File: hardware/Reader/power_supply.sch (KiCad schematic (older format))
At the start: 4 parts

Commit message: Revising reader
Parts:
- added J_PS_2, J_PS_3: 1546931-2, footprints:1546931-2, symbol 1546931-2:1546931-2
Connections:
- net +12V: now also J_PS_1.1
- net +3V3: now also J_PS_3.1; no longer J_PS_1.2
- net +5V: now also J_PS_2.1; no longer J_PS_1.1
- net GND: now also J_PS_1.2, J_PS_2.2, J_PS_3.2
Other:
- moved on the sheet: J_PS_1
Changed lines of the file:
@@
 $Descr USLetter 11000 8500
 encoding utf-8
-Sheet 15 19
+Sheet 13 19
 Title "CANnect Reader | Power Supply"
-Date "2020-10-28"
-Rev "0.0.04"
+Date "2020-11-19"
+Rev "0.0.05"
 Comp "CANtech"
 Comment1 "Created by Choong Jin Ng | jin8383@gmail.com"
@@
 $EndComp
 Wire Wire Line
-	3350 3500 3350 4350
+	3350 3500 3350 3700
 $Sheet
 S 1700 2450 1500 750
@@
 	6850 3550 6850 3400
 Wire Wire Line
-	6850 2500 6850 2350
-Wire Wire Line
 	6850 4000 6850 3850
 $Comp
@@
 NoConn ~ 6450 2000
 Connection ~ 6850 3400
-Wire Wire Line
-	7250 3400 7250 2600
-Wire Wire Line
-	6850 3400 7250 3400
 Connection ~ 6850 1900
-Wire Wire Line
-	7250 1900 7250 2500
-Wire Wire Line
-	6850 1900 7250 1900
 Wire Wire Line
 	6850 1900 6850 1650
@@
 L 1546931-2:1546931-2 J_PS_1
 U 1 1 5FA002EC
-P 7850 2600
-F 0 "J_PS_1" H 8080 2696 50  0000 L CNN
-F 1 "1546931-2" H 8080 2605 50  0000 L CNN
-F 2 "footprints:1546931-2" H 7850 2600 50  0001 L BNN
-F 3 "https://www.te.com/commerce/DocumentDelivery/DDEController?Action=srchrtrv&DocNm=1-1773458-1_EURO_STYLE_QRG&DocType=DS&DocLang=English" H 7850 2600 50  0001 L BNN
-F 4 "1546931-2" H 7850 2600 50  0001 C CNN "Part Name"
-F 5 "TE Connectivity AMP Connectors" H 7850 2600 50  0001 C CNN "Manufacturer"
-F 6 "Digikey Canada" H 7850 2600 50  0001 C CNN "Vendor"
-F 7 "A97965-ND" H 7850 2600 50  0001 C CNN "digikeypn"
-	1    7850 2600
-	1    0    0    -1
-$EndComp
-Wire Wire Line
-	7250 2500 7450 2500
-Wire Wire Line
-	7450 2600 7250 2600
-Wire Wire Line
-	3350 2800 4850 2800
+P 4250 3700
+F 0 "J_PS_1" H 4480 3796 50  0000 L CNN
+F 1 "1546931-2" H 4480 3705 50  0000 L CNN
+F 2 "footprints:1546931-2" H 4250 3700 50  0001 L BNN
+F 3 "https://www.te.com/commerce/DocumentDelivery/DDEController?Action=srchrtrv&DocNm=1-1773458-1_EURO_STYLE_QRG&DocType=DS&DocLang=English" H 4250 3700 50  0001 L BNN
+F 4 "1546931-2" H 4250 3700 50  0001 C CNN "Part Name"
+F 5 "TE Connectivity AMP Connectors" H 4250 3700 50  0001 C CNN "Manufacturer"
+F 6 "Digikey Canada" H 4250 3700 50  0001 C CNN "Vendor"
+F 7 "A97965-ND" H 4250 3700 50  0001 C CNN "digikeypn"
+	1    4250 3700
+	1    0    0    -1
+$EndComp
+Wire Wire Line
+	3350 2800 3850 2800
 Wire Wire Line
 	3300 5150 6000 5150
+$Comp
+L 1546931-2:1546931-2 J_PS_2
+U 1 1 5FBD8B3B
+P 7850 2000
+F 0 "J_PS_2" H 8080 2096 50  0000 L CNN
+F 1 "1546931-2" H 8080 2005 50  0000 L CNN
+F 2 "footprints:1546931-2" H 7850 2000 50  0001 L BNN
+F 3 "https://www.te.com/commerce/DocumentDelivery/DDEController?Action=srchrtrv&DocNm=1-1773458-1_EURO_STYLE_QRG&DocType=DS&DocLang=English" H 7850 2000 50  0001 L BNN
+F 4 "1546931-2" H 7850 2000 50  0001 C CNN "Part Name"
+F 5 "TE Connectivity AMP Connectors" H 7850 2000 50  0001 C CNN "Manufacturer"
+F 6 "Digikey Canada" H 7850 2000 50  0001 C CNN "Vendor"
+F 7 "A97965-ND" H 7850 2000 50  0001 C CNN "digikeypn"
+	1    7850 2000
+	1    0    0    -1
+$EndComp
+$Comp
+L 1546931-2:1546931-2 J_PS_3
+U 1 1 5FBD9454
+P 7850 3500
+F 0 "J_PS_3" H 8080 3596 50  0000 L CNN
+F 1 "1546931-2" H 8080 3505 50  0000 L CNN
+F 2 "footprints:1546931-2" H 7850 3500 50  0001 L BNN
+F 3 "https://www.te.com/commerce/DocumentDelivery/DDEController?Action=srchrtrv&DocNm=1-1773458-1_EURO_STYLE_QRG&DocType=DS&DocLang=English" H 7850 3500 50  0001 L BNN
+F 4 "1546931-2" H 7850 3500 50  0001 C CNN "Part Name"
+F 5 "TE Connectivity AMP Connectors" H 7850 3500 50  0001 C CNN "Manufacturer"
+F 6 "Digikey Canada" H 7850 3500 50  0001 C CNN "Vendor"
+F 7 "A97965-ND" H 7850 3500 50  0001 C CNN "digikeypn"
+	1    7850 3500
+	1    0    0    -1
+$EndComp
+Wire Wire Line
+	6850 1900 7450 1900
+Wire Wire Line
+	3850 3600 3850 2800
+Connection ~ 3850 2800
+Wire Wire Line
+	3850 2800 4850 2800
+Wire Wire Line
+	3850 3700 3350 3700
+Connection ~ 3350 3700
+Wire Wire Line
+	3350 3700 3350 4350
+Wire Wire Line
+	6850 3400 7450 3400
+Wire Wire Line
+	6850 2350 6850 2500
+Wire Wire Line
+	6850 2500 7450 2500
+Wire Wire Line
+	7450 2500 7450 2000
+Connection ~ 6850 2500
+Wire Wire Line
+	6850 4000 7450 4000
+Wire Wire Line
+	7450 4000 7450 3500
+Connection ~ 6850 4000
 $EndSCHEMATC

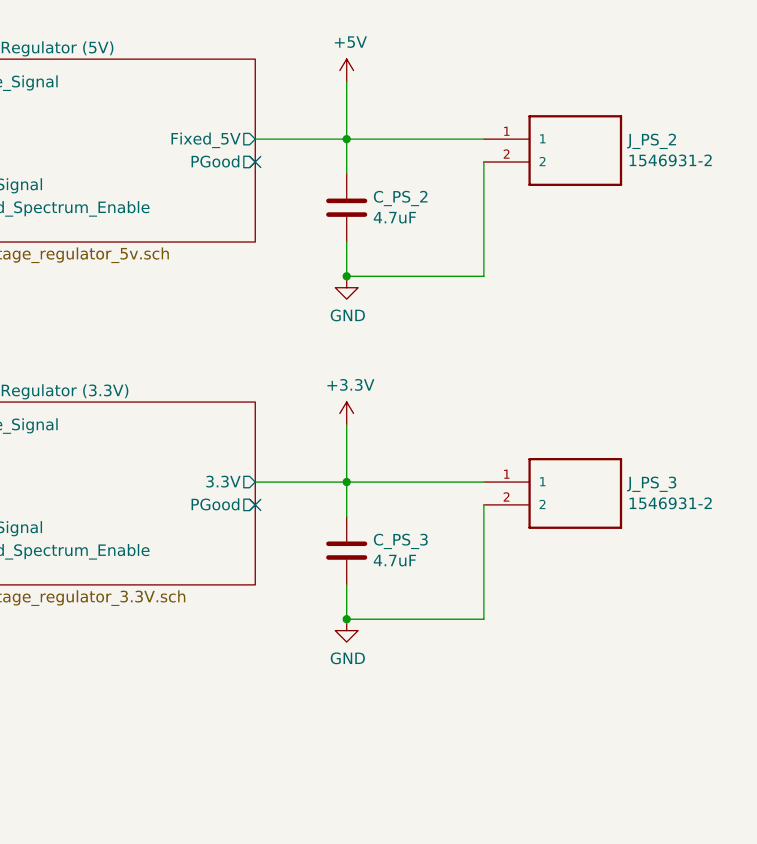
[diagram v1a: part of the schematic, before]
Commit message: Fixed numerous bugs in design for Reader Schematic and PCB
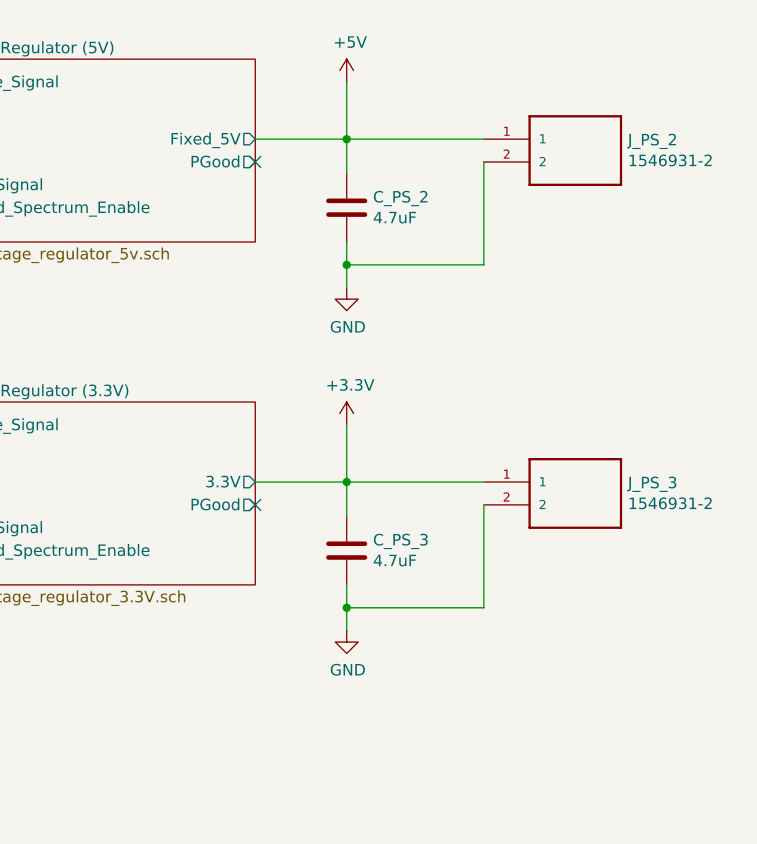
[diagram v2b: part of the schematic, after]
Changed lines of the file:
@@
 $Descr USLetter 11000 8500
 encoding utf-8
-Sheet 13 19
+Sheet 15 19
 Title "CANnect Reader | Power Supply"
 Date "2020-11-19"
@@
 L power:GND #PWR096
 U 1 1 5F96A5B0
-P 6850 4000
-F 0 "#PWR096" H 6850 3750 50  0001 C CNN
-F 1 "GND" H 6855 3827 50  0000 C CNN
-F 2 "" H 6850 4000 50  0001 C CNN
-F 3 "" H 6850 4000 50  0001 C CNN
-	1    6850 4000
+P 6850 4050
+F 0 "#PWR096" H 6850 3800 50  0001 C CNN
+F 1 "GND" H 6855 3877 50  0000 C CNN
+F 2 "" H 6850 4050 50  0001 C CNN
+F 3 "" H 6850 4050 50  0001 C CNN
+	1    6850 4050
 	1    0    0    -1
 $EndComp
@@
 	6850 3550 6850 3400
 Wire Wire Line
-	6850 4000 6850 3850
+	6850 4050 6850 3950
 $Comp
 L power:GND #PWR094
 U 1 1 5F9698CD
-P 6850 2500
-F 0 "#PWR094" H 6850 2250 50  0001 C CNN
-F 1 "GND" H 6855 2327 50  0000 C CNN
-F 2 "" H 6850 2500 50  0001 C CNN
-F 3 "" H 6850 2500 50  0001 C CNN
-	1    6850 2500
+P 6850 2550
+F 0 "#PWR094" H 6850 2300 50  0001 C CNN
+F 1 "GND" H 6855 2377 50  0000 C CNN
+F 2 "" H 6850 2550 50  0001 C CNN
+F 3 "" H 6850 2550 50  0001 C CNN
+	1    6850 2550
 	1    0    0    -1
 $EndComp
@@
 	6850 3400 7450 3400
 Wire Wire Line
-	6850 2350 6850 2500
-Wire Wire Line
-	6850 2500 7450 2500
-Wire Wire Line
-	7450 2500 7450 2000
-Connection ~ 6850 2500
-Wire Wire Line
-	6850 4000 7450 4000
-Wire Wire Line
-	7450 4000 7450 3500
-Connection ~ 6850 4000
+	6850 2350 6850 2450
+Wire Wire Line
+	6850 3950 7450 3950
+Connection ~ 6850 3950
+Wire Wire Line
+	6850 3950 6850 3850
+Wire Wire Line
+	7450 3950 7450 3500
+Wire Wire Line
+	6850 2450 7450 2450
+Connection ~ 6850 2450
+Wire Wire Line
+	6850 2450 6850 2550
+Wire Wire Line
+	7450 2450 7450 2000
 $EndSCHEMATC

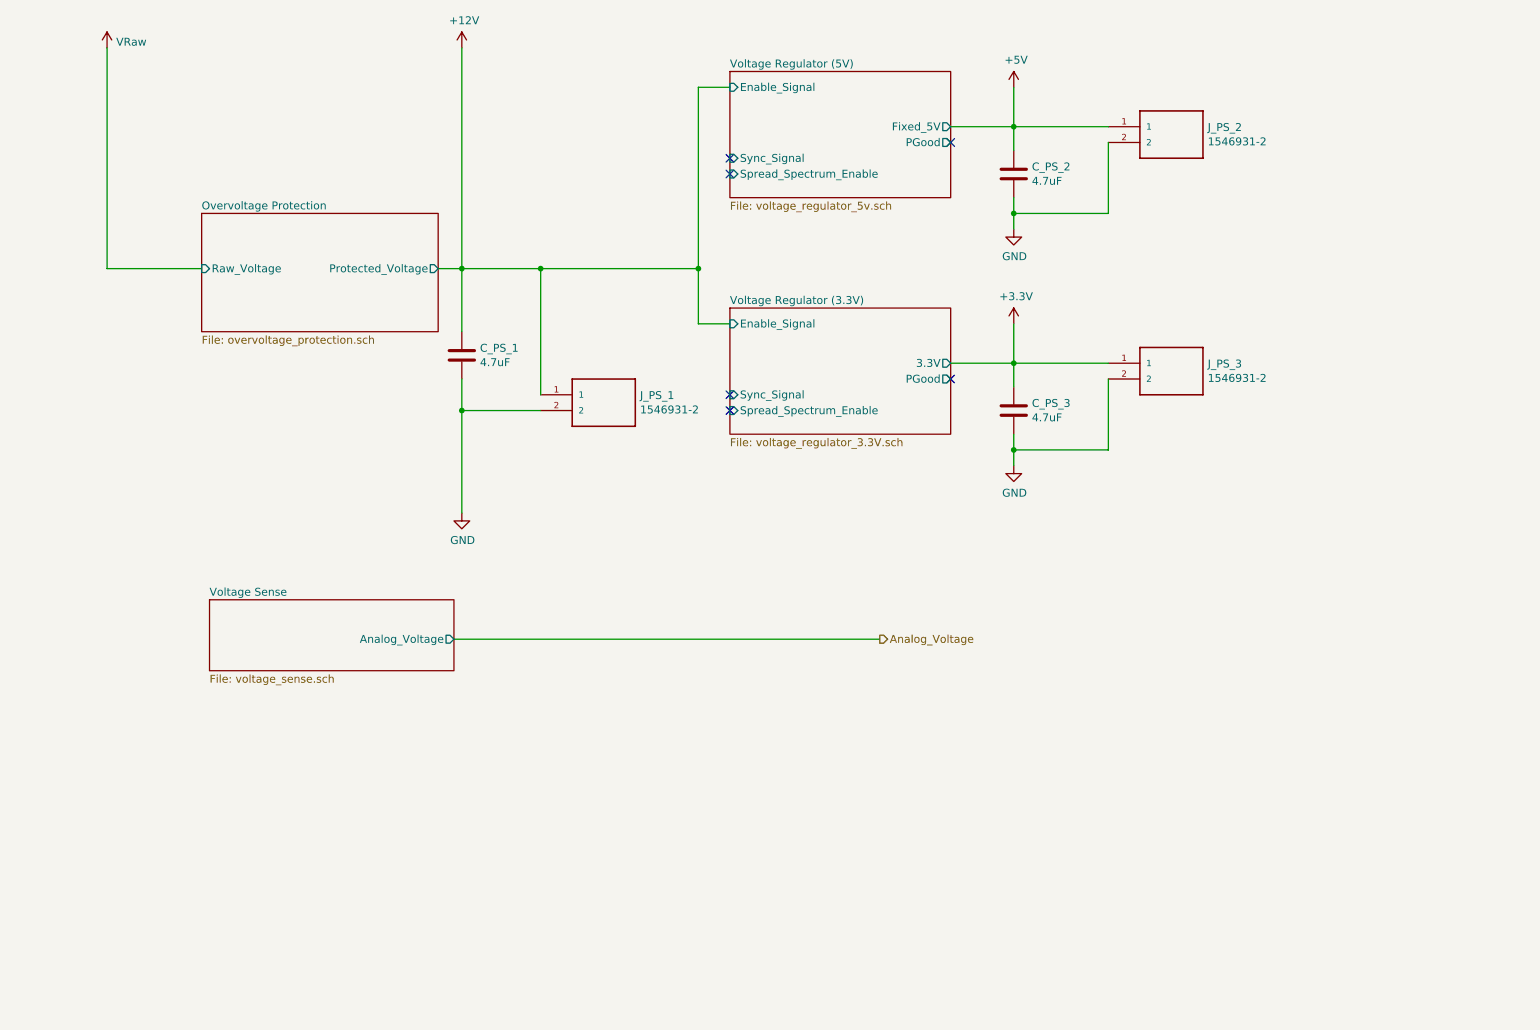
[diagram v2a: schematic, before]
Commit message: Updated reader schematic to v0.0.5 by adding ESP32, removing unused transceivers, fixed design flaws, increased header pins and fixed footprints. Working on reader PCB design
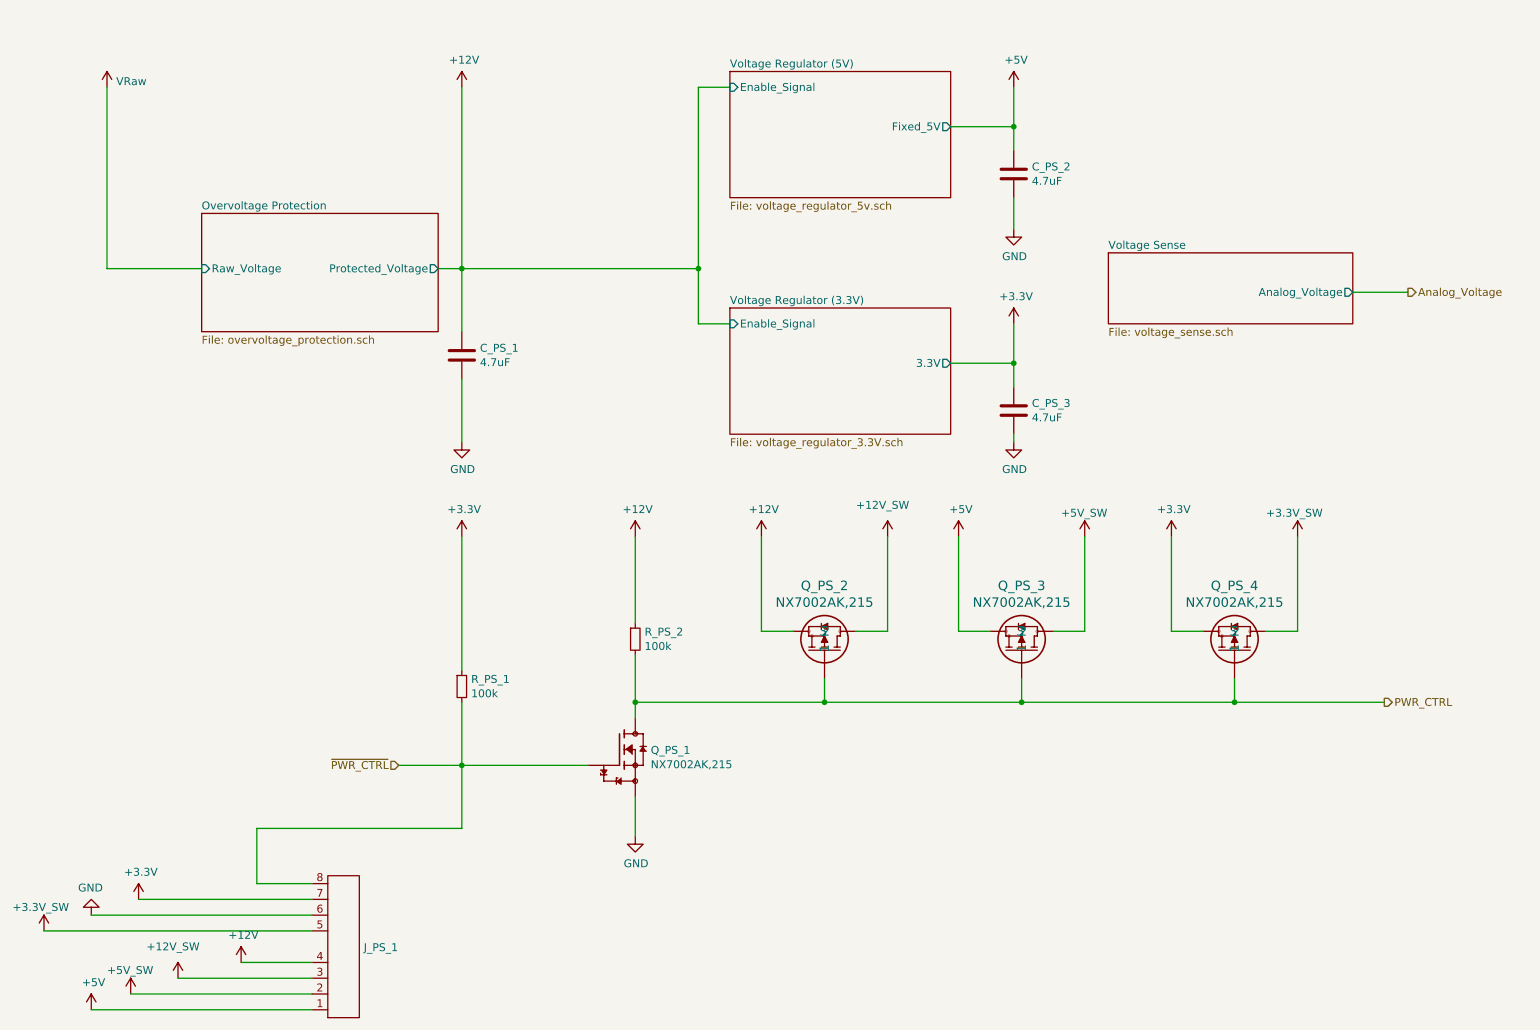
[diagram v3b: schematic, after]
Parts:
- removed J_PS_1, J_PS_2, J_PS_3: 1546931-2, footprints:1546931-2, symbol 1546931-2:1546931-2
- added J_PS_1: Header_Pin_8, Connector_PinHeader_2.54mm:PinHeader_1x08_P2.54mm_Vertical, symbol CANtech:Header_Pin_8
- added Q_PS_1: NX7002AK,215, footprints:SOT95P230X110-3N, symbol NX7002AK_215:NX7002AK,215
- added Q_PS_2, Q_PS_3, Q_PS_4: NX7002AK,215, footprints:SOT95P230X110-3N, symbol IRLML5103TRPBF:IRLML5103TRPBF
- added R_PS_1, R_PS_2: 100k, footprints:RESC1608X55N, symbol Device:R_Small
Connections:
- net +12V: now also J_PS_1.4, Q_PS_2.3, R_PS_2.1
- net +3V3: now also J_PS_1.7, Q_PS_4.3, R_PS_1.1
- net +5V: now also J_PS_1.1, Q_PS_3.3
- net GND: now also J_PS_1.6, Q_PS_1.2
- new net +12V_SW: J_PS_1.3, Q_PS_2.2
- new net +3.3V_SW: J_PS_1.5, Q_PS_4.2
- new net +5V_SW: J_PS_1.2, Q_PS_3.2
- new net PWR_CTRL: Q_PS_1.3, Q_PS_2.1, Q_PS_3.1, Q_PS_4.1, R_PS_2.2
- new net ~PWR_CTRL~: J_PS_1.8, Q_PS_1.1, R_PS_1.2
- no-connect marks 6 -> 0
